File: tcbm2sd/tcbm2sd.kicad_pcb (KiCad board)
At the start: 2 copper layers, 56 x 91 mm, 30 parts, among them J1 TCBM, J2 JTAG, J3 GPIO, J4 AMS1117, J5 SD CARD, J7 ALT_A6_A7, SW1 BUT_PREV, SW2 BUT_NEXT, U1 XC9572XL-VQ64, U2 Arduino Pro Mini, U3 AMS1117-3.3, U4 27C512, U5 74HC00

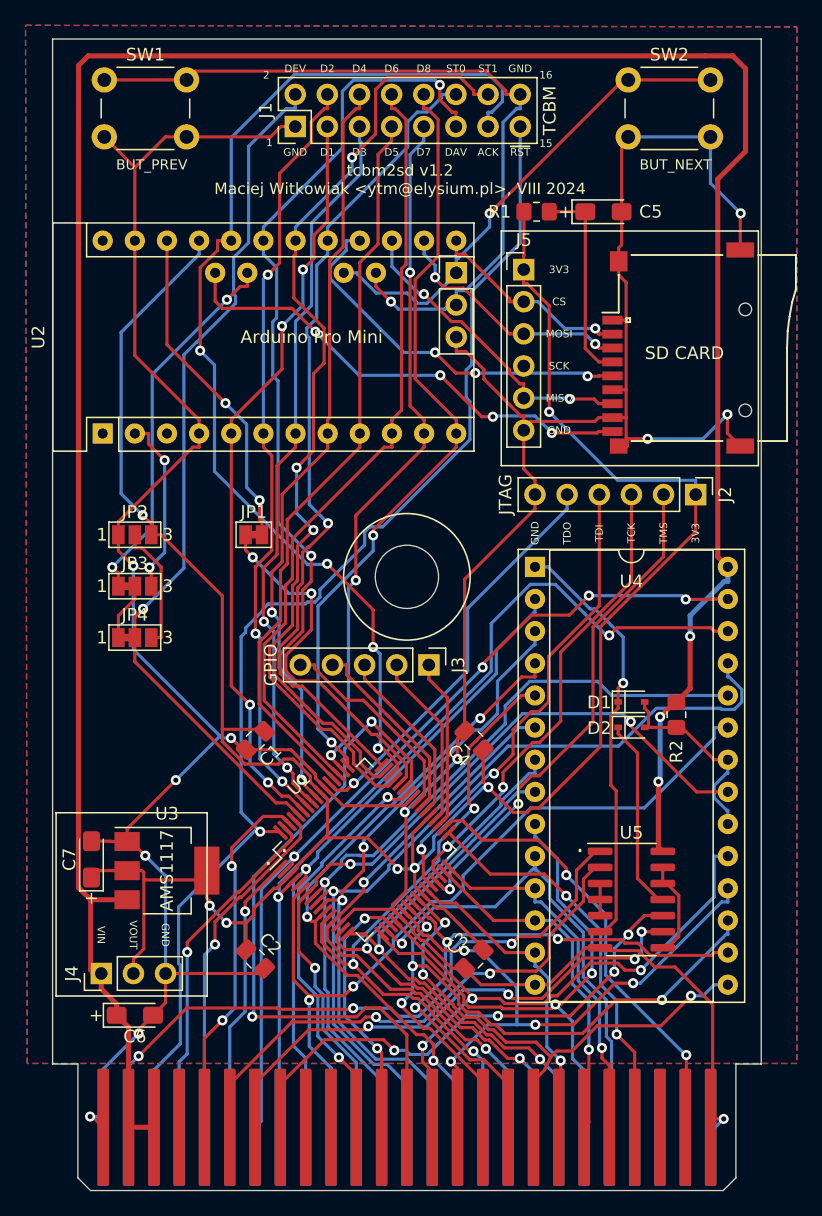
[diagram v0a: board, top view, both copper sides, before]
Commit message: remove GPIO connector, 74'00, diodes and pullup; added pullups for A6/A7; JP1 (reset passthrough) default open; bump revision to 1.3
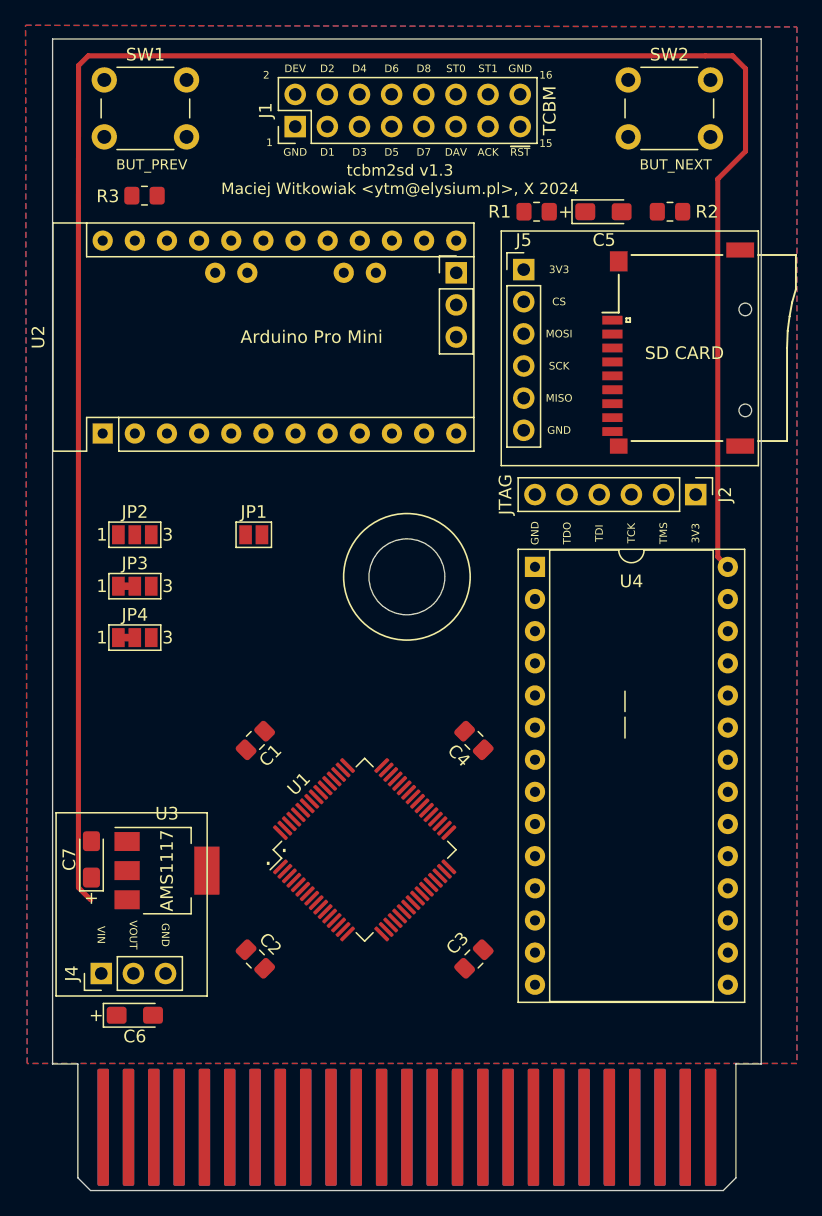
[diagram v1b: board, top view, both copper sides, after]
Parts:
- removed D1, D2: 1N4148WS, Diode_SMD:D_SOD-323
- removed J3: GPIO, Connector_PinHeader_2.54mm:PinHeader_1x05_P2.54mm_Vertical
- removed U5: 74HC00, Package_SO:SO-14_3.9x8.65mm_P1.27mm
- added R3: 10K, Resistor_SMD:R_0805_2012Metric_Pad1.20x1.40mm_HandSolder, F.Cu at (127.8, 71.9)
- JP1: value SolderJumper_2_Bridged -> SolderJumper_2_Open; footprint Jumper:SolderJumper-2_P1.3mm_Bridged_Pad1.0x1.5mm -> Jumper:SolderJumper-2_P1.3mm_Open_Pad1.0x1.5mm
- moved R2 39.8 mm to (169.3, 73.2), turned to 180 degrees
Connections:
- R2 pad 1: /~{ROMCS} -> +3V3
- R2 pad 2: /VCC -> /ALT_A7
- U$1 pad 11: /~{CAS} -> unconnected-(U$1-Pad11)
- U1 pad 35: Net-(J3-Pad1) -> /C1LO
- U1 pad 36: Net-(J3-Pad2) -> /C1HI
- U1 pad 38: Net-(J3-Pad3) -> /C2LO
- U1 pad 39: Net-(J3-Pad4) -> /C2HI
- U1 pad 40: Net-(J3-Pad5) -> /ROM_A15
- U1 pad 42: /~{CAS} -> /~{ROMCS}
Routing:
- net GND: track 299.5 -> 0.00 mm, vias 12 -> 0
- net +3V3: track 198.7 -> 0.00 mm, vias 7 -> 0
- net /~{RESET}: track 97.0 -> 0.00 mm, vias 1 -> 0
- net /ACK: track 87.6 -> 0.00 mm, vias 4 -> 0
- net /STATUS1: track 77.3 -> 0.00 mm, vias 3 -> 0
- net /DAV: track 74.3 -> 0.00 mm, vias 2 -> 0
- net /A13: track 70.6 -> 0.00 mm, vias 2 -> 0
- net /DEV: track 68.6 -> 0.00 mm, vias 1 -> 0
- net /A14: track 67.3 -> 0.00 mm, vias 4 -> 0
- net /STATUS0: track 67.2 -> 0.00 mm, vias 1 -> 0
- net /A11: track 63.7 -> 0.00 mm, vias 2 -> 0
- net /A10: track 62.8 -> 0.00 mm, vias 3 -> 0
- net /A8: track 62.3 -> 0.00 mm, vias 1 -> 0
- net /DIO6: track 61.8 -> 0.00 mm
- net /ALT_A6: track 61.4 -> 0.00 mm, vias 1 -> 0
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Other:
- board text added: "tcbm2sd v1.3 Maciej Witkowiak <ytm@elysium.pl>, X 2024"
- board text removed: "tcbm2sd v1.2 Maciej Witkowiak <ytm@elysium.pl>, VIII 2024"

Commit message: updated routing
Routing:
- net GND: track 0.00 -> 313.4 mm, vias 0 -> 22
- net +3V3: track 0.00 -> 196.3 mm, vias 0 -> 4
- net /~{RESET}: track 0.00 -> 92.2 mm, vias 0 -> 1
- net /ACK: track 0.00 -> 75.3 mm, vias 0 -> 2
- net /A10: track 0.00 -> 70.0 mm, vias 0 -> 2
- net /STATUS1: track 0.00 -> 69.7 mm, vias 0 -> 3
- net /ALT_A6: track 0.00 -> 69.4 mm
- net /A13: track 0.00 -> 69.0 mm, vias 0 -> 1
- net /DEV: track 0.00 -> 68.9 mm, vias 0 -> 3
- net /A14: track 0.00 -> 68.6 mm, vias 0 -> 2
- net /DAV: track 0.00 -> 67.7 mm, vias 0 -> 3
- net /A9: track 0.00 -> 64.2 mm, vias 0 -> 3
- net /STATUS0: track 0.00 -> 63.2 mm, vias 0 -> 3
- net /DIO2: track 0.00 -> 60.1 mm, vias 0 -> 1
- net /A11: track 0.00 -> 59.5 mm, vias 0 -> 3
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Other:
- board text added: "32K: $0000-$7FFF C1 64K: $0000-$7FFF C2 $8000-$FFFF C1"

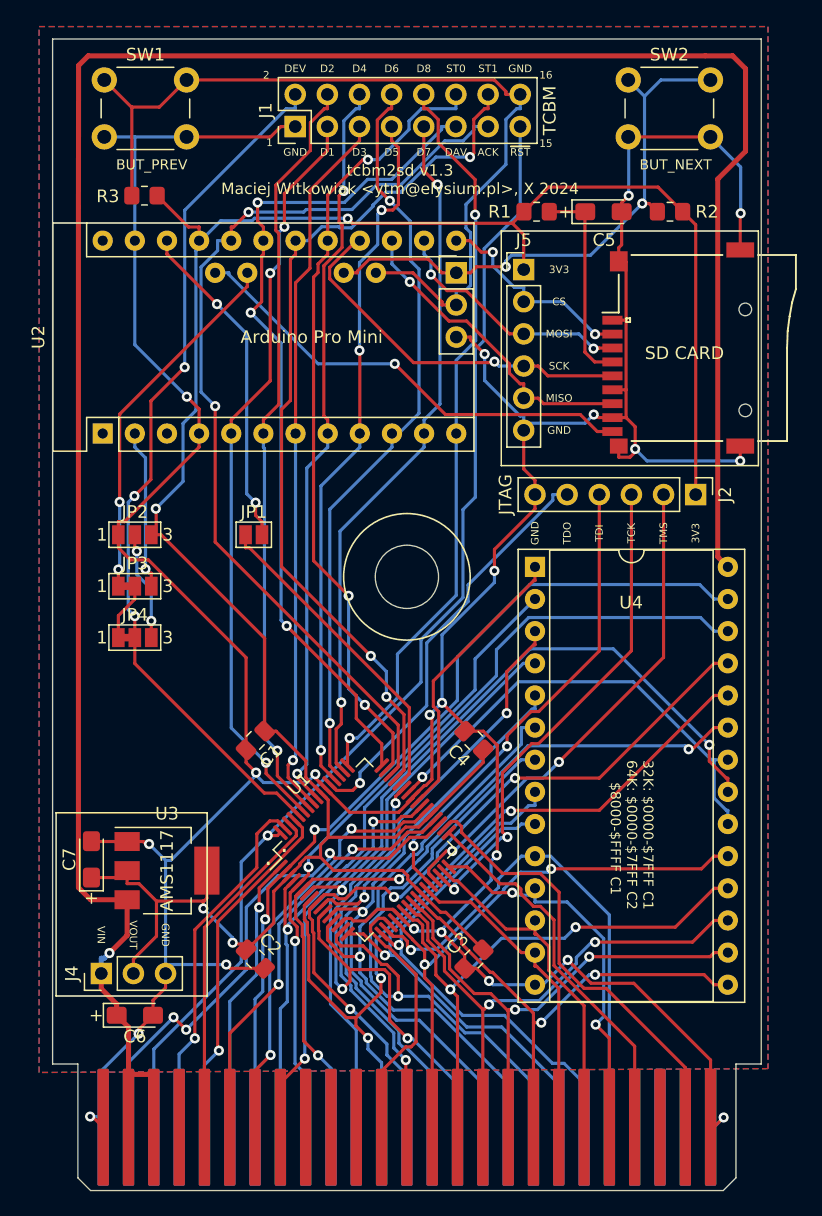
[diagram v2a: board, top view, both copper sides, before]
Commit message: dual footprint for pushbutton switch straight or angled
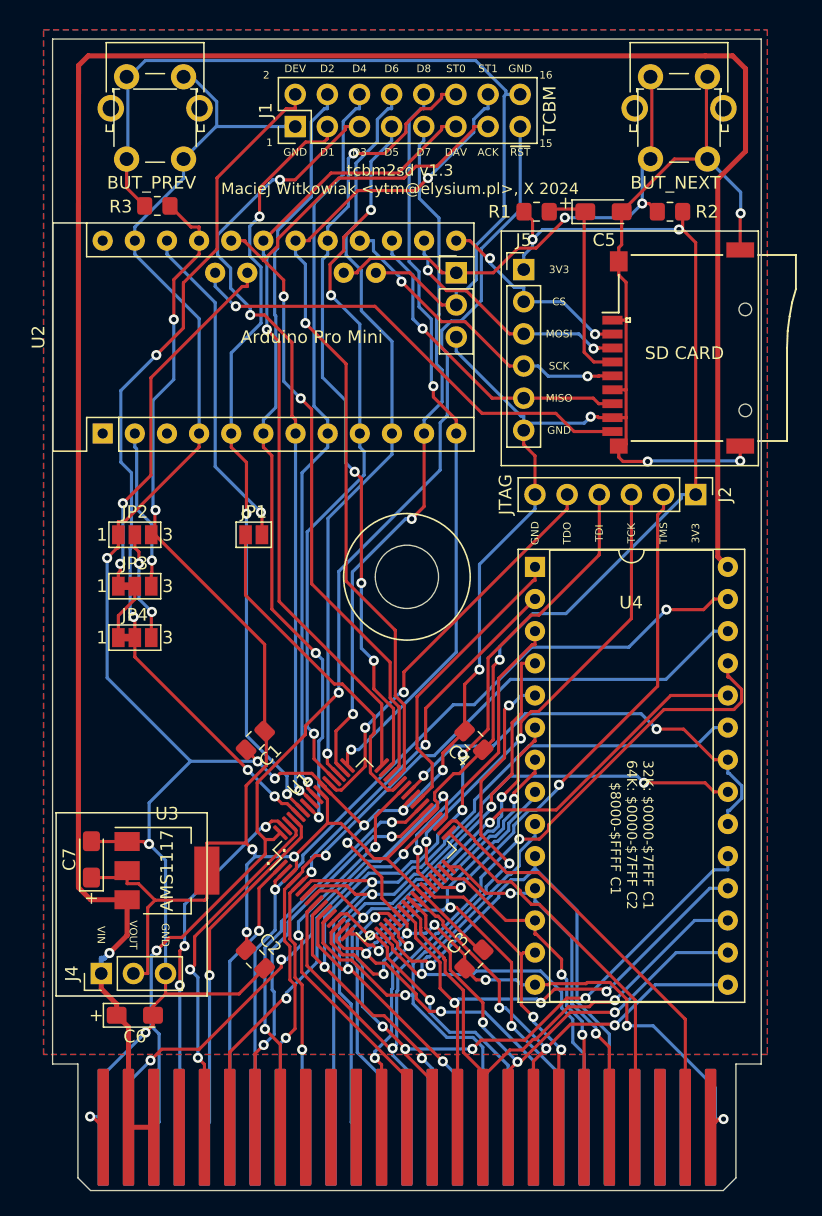
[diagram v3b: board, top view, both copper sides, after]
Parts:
- SW1, SW2: footprint Button_Switch_THT:SW_PUSH_6mm -> LittleSixteen:SW_PUSH_6mm_OR_SW_Tactile_SPST_Angled_PTS645Vx58-2LFS
- moved SW1 1.42 mm to (124.6, 64.2)
- moved SW2 1.42 mm to (166.0, 64.2)
- moved R3 1.30 mm to (128.8, 72.7)
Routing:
- net /A10: track 70.0 -> 58.9 mm
- net /A5: track 45.1 -> 55.5 mm, vias 1 -> 3
- net /A8: track 58.6 -> 68.1 mm, vias 3 -> 2
- net /A7: track 48.2 -> 57.4 mm, vias 2 -> 3
- net /A9: track 64.2 -> 55.2 mm, vias 3 -> 2
- net GND: track 313.4 -> 305.2 mm, vias 22 -> 21
- net /A1: track 36.5 -> 43.8 mm
- net /DIO3: track 56.4 -> 63.5 mm, vias 1 -> 3
- net /ALT_A7: track 44.7 -> 37.9 mm
- net /A13: track 69.0 -> 63.5 mm, vias 1 -> 2
- net /D7: track 45.1 -> 50.4 mm, vias 2 -> 5
- net /SD_SCK: track 29.5 -> 25.0 mm, vias 1 -> 2
- net /A6: track 55.0 -> 50.8 mm, vias 2 -> 3
- net /ACK: track 75.3 -> 71.2 mm
- net /C2HI: track 28.1 -> 32.2 mm
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
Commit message: v1.4 with correct silkscreen info about C1/C2 ROM banks and 3.3V /RESET routed to TCBM connector instead of 5V /RESET
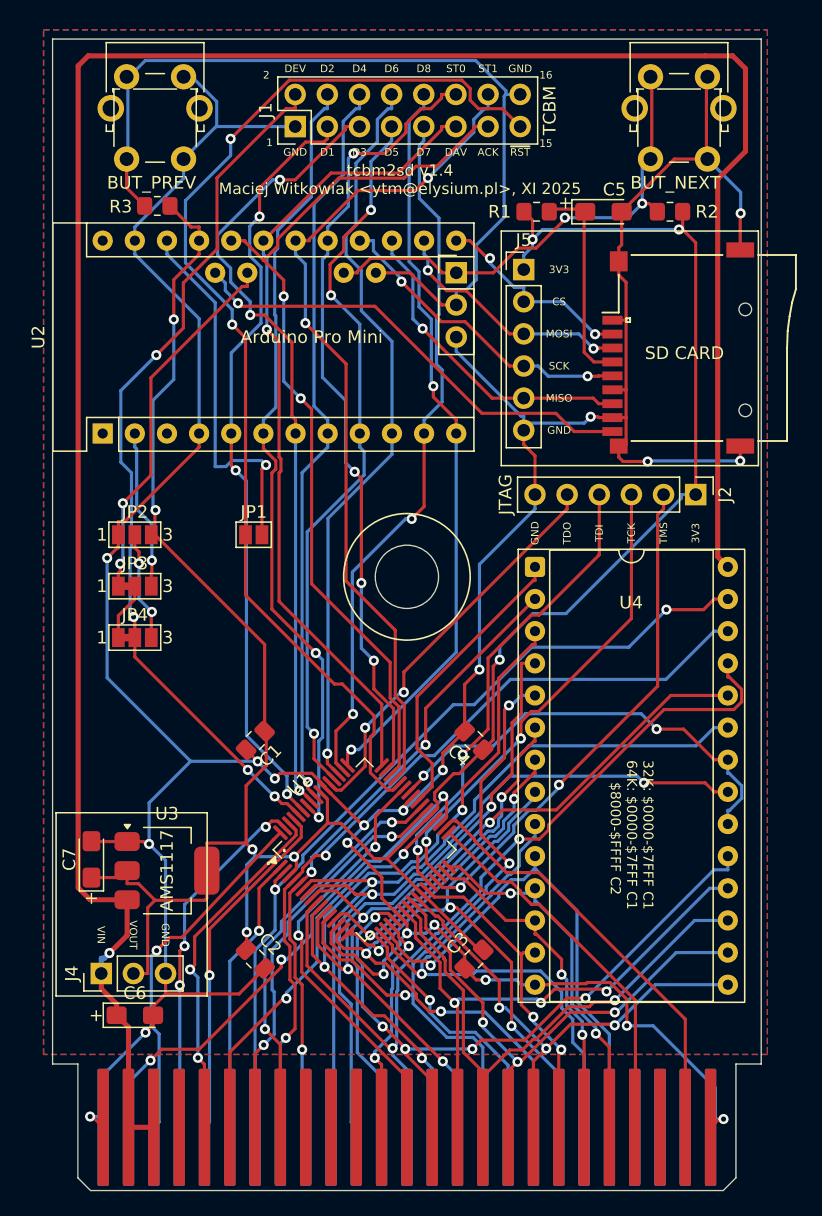
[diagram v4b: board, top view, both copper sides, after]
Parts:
- C5, C6, C7: footprint Capacitor_Tantalum_SMD:CP_EIA-3216-12_Kemet-S_Pad1.58x1.35mm_HandSolder -> Capacitor_Tantalum_SMD:CP_EIA-3216-12_Kemet-S_HandSolder
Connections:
- J1 pad 15: /~{RESET} -> /~{RESET_3_3V}
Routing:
- net /~{RESET}: track 94.9 -> 28.4 mm, vias 2 -> 1
- net /~{RESET_3_3V}: track 26.6 -> 88.2 mm, vias 0 -> 2
- net Net-(JP1-B): track 26.4 -> 29.4 mm
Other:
- board text added: "32K: $0000-$7FFF C1 64K: $0000-$7FFF C1 $8000-$FFFF C2"
- board text added: "tcbm2sd v1.4 Maciej Witkowiak <ytm@elysium.pl>, XI 2025"
- board text removed: "32K: $0000-$7FFF C1 64K: $0000-$7FFF C2 $8000-$FFFF C1"
- board text removed: "tcbm2sd v1.3 Maciej Witkowiak <ytm@elysium.pl>, X 2024"
